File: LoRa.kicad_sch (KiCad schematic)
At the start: 4 parts

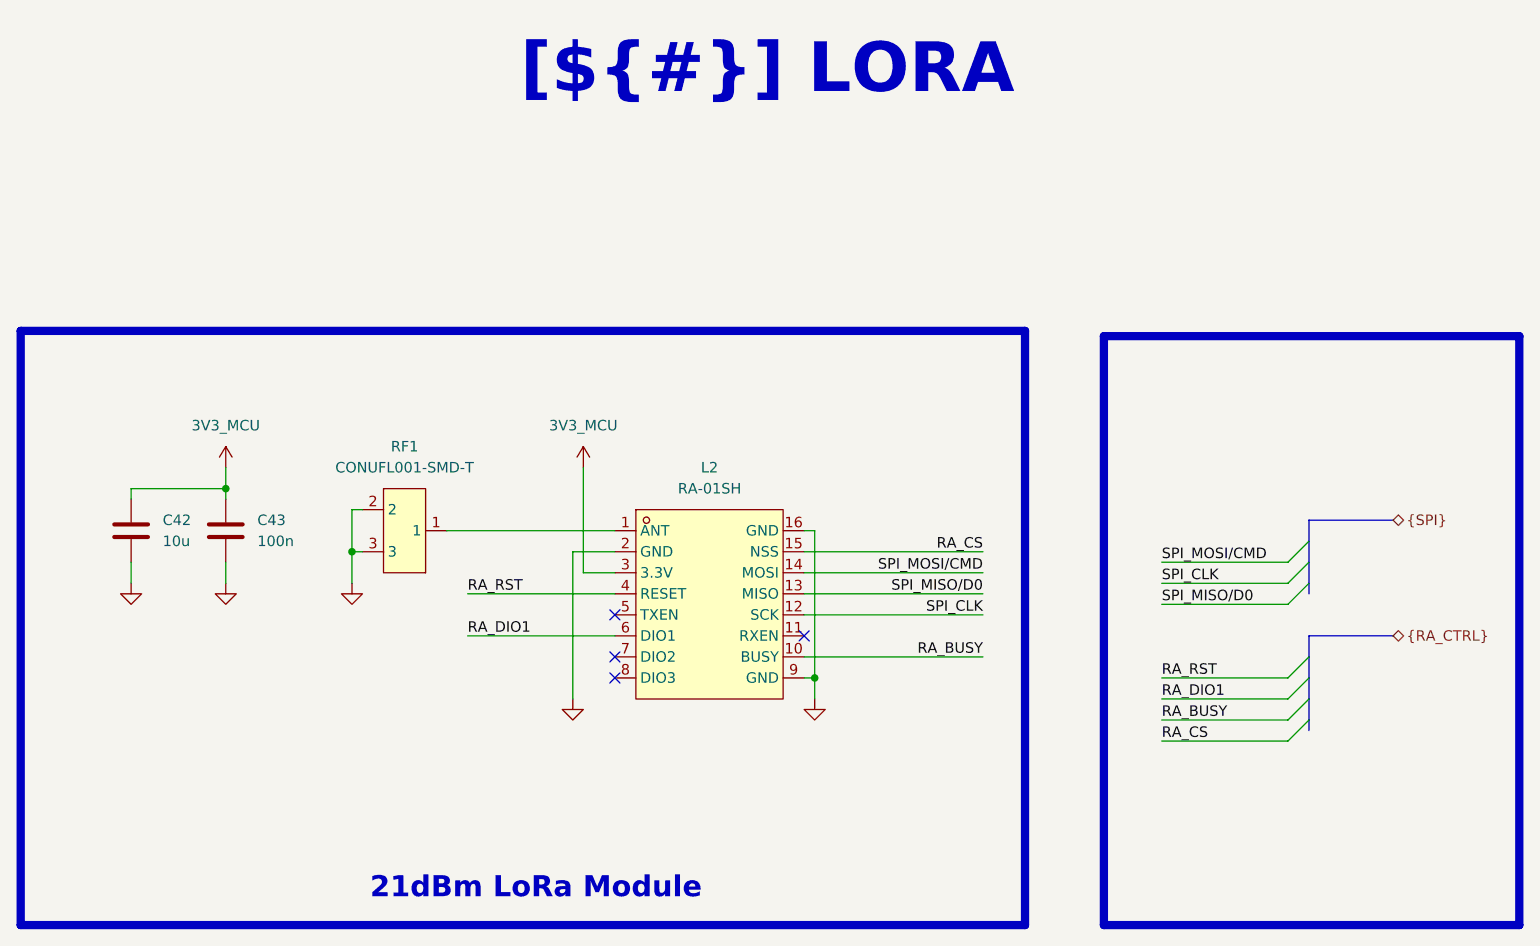
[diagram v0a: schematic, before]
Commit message: [Schematic][Added] Project Architecture, connectors
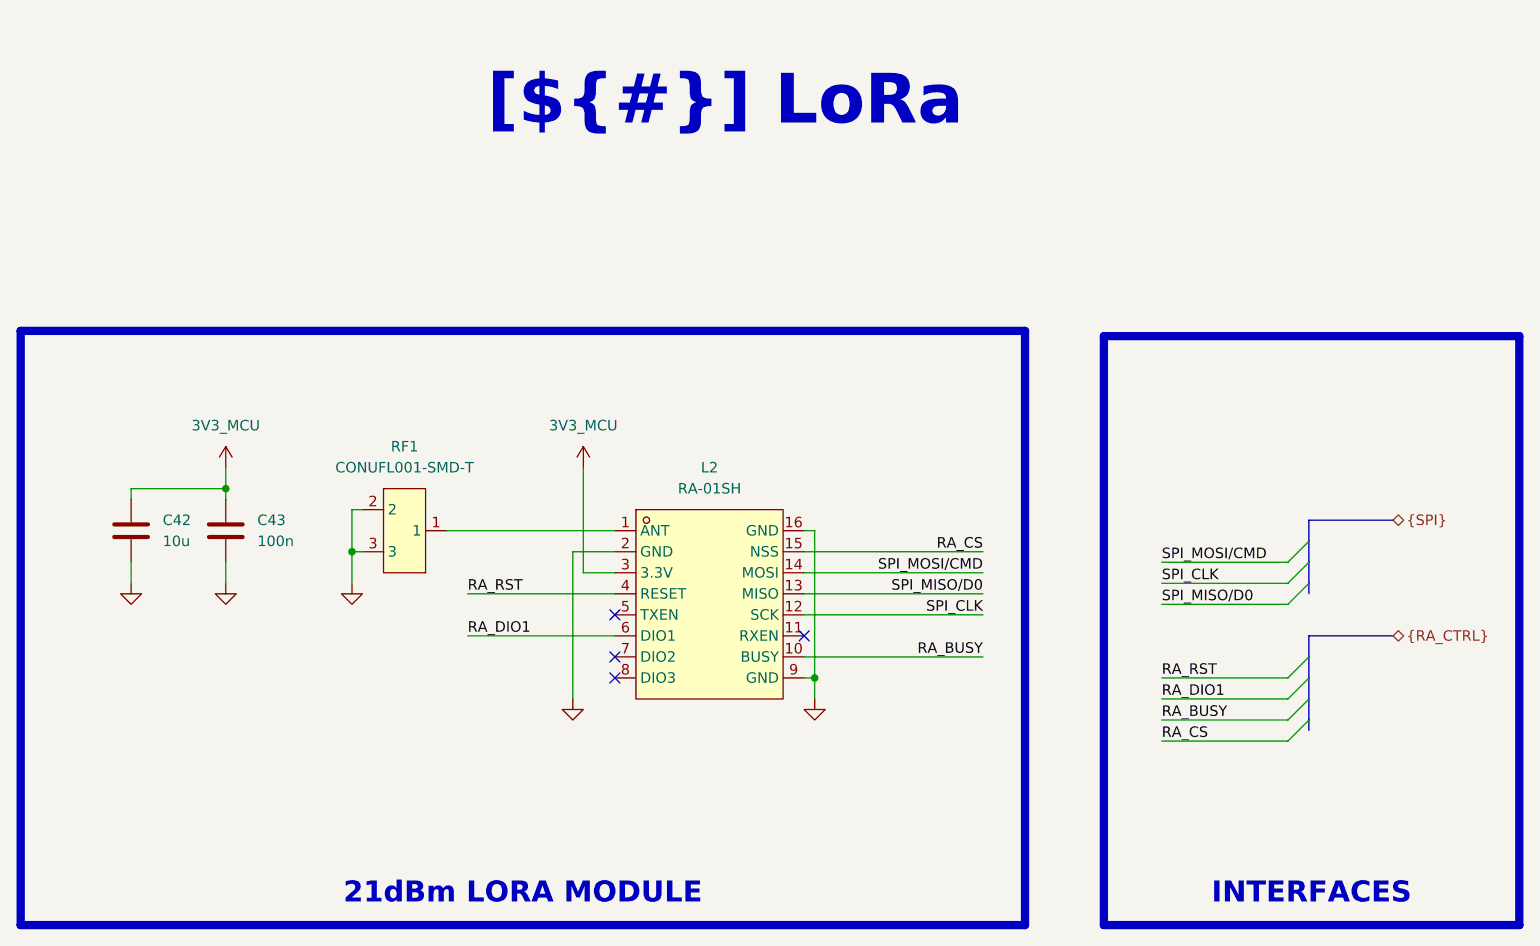
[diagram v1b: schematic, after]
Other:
- title: LORA -> LoRa
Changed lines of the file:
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@@
 	(paper "A4")
 	(title_block
-		(title "LORA")
+		(title "LoRa")
 		(date "2025-01-12")
 		(rev "${REVISION}")
@@
 	(text_box "[${#}] ${TITLE}"
 		(exclude_from_sim no)
-		(at 115.57 15.24 0)
+		(at 110.49 19.05 0)
 		(size 72.39 12.7)
 		(margins 4.4999 4.4999 4.4999 4.4999)
@@
 		)
 	)
-	(text_box "21dBm LoRa Module\n"
+	(text_box "21dBm LORA MODULE\n"
 		(exclude_from_sim no)
-		(at 100.965 116.205 0)
-		(size 45.72 7.62)
+		(at 62.23 116.84 0)
+		(size 120.015 7.62)
 		(margins 1.9049 1.9049 1.9049 1.9049)
 		(stroke
+			(width -0.0001)
+			(type solid)
+		)
+		(fill
+			(type none)
+		)
+		(effects
+			(font
+				(face "Times New Roman")
+				(size 2.54 2.54)
+				(thickness 0.508)
+				(bold yes)
+				(color 162 22 34 1)
+			)
+			(justify bottom)
+		)
+	)
+	(text_box "INTERFACES\n"
+		(exclude_from_sim no)
+		(at 193.04 116.84 0)
+		(size 48.895 7.62)
+		(margins 1.9049 1.9049 1.9049 1.9049)
+		(stroke

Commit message: [PCB/SCH][Added] Preliminary version
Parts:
- added D3: PESD0402-140, easyeda2kicad:D0402-BI, symbol easyeda2kicad:PESD0402-140
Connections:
- net GND: now also D3.1
- net at L2.1 (ANT), RF1.1: now also D3.2
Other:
- moved on the sheet: C42, C43, RF1
